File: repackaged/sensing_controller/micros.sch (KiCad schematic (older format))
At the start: 27 parts, among them J4 CONN_02X03, J5 CONN_02X03, U10 TXB0104, U7 ATMEGA16M1, U8 MCP2561-E_SN, U9 ATmega328P-AU, Y3 Crystal_SMD, Y4 Crystal_SMD

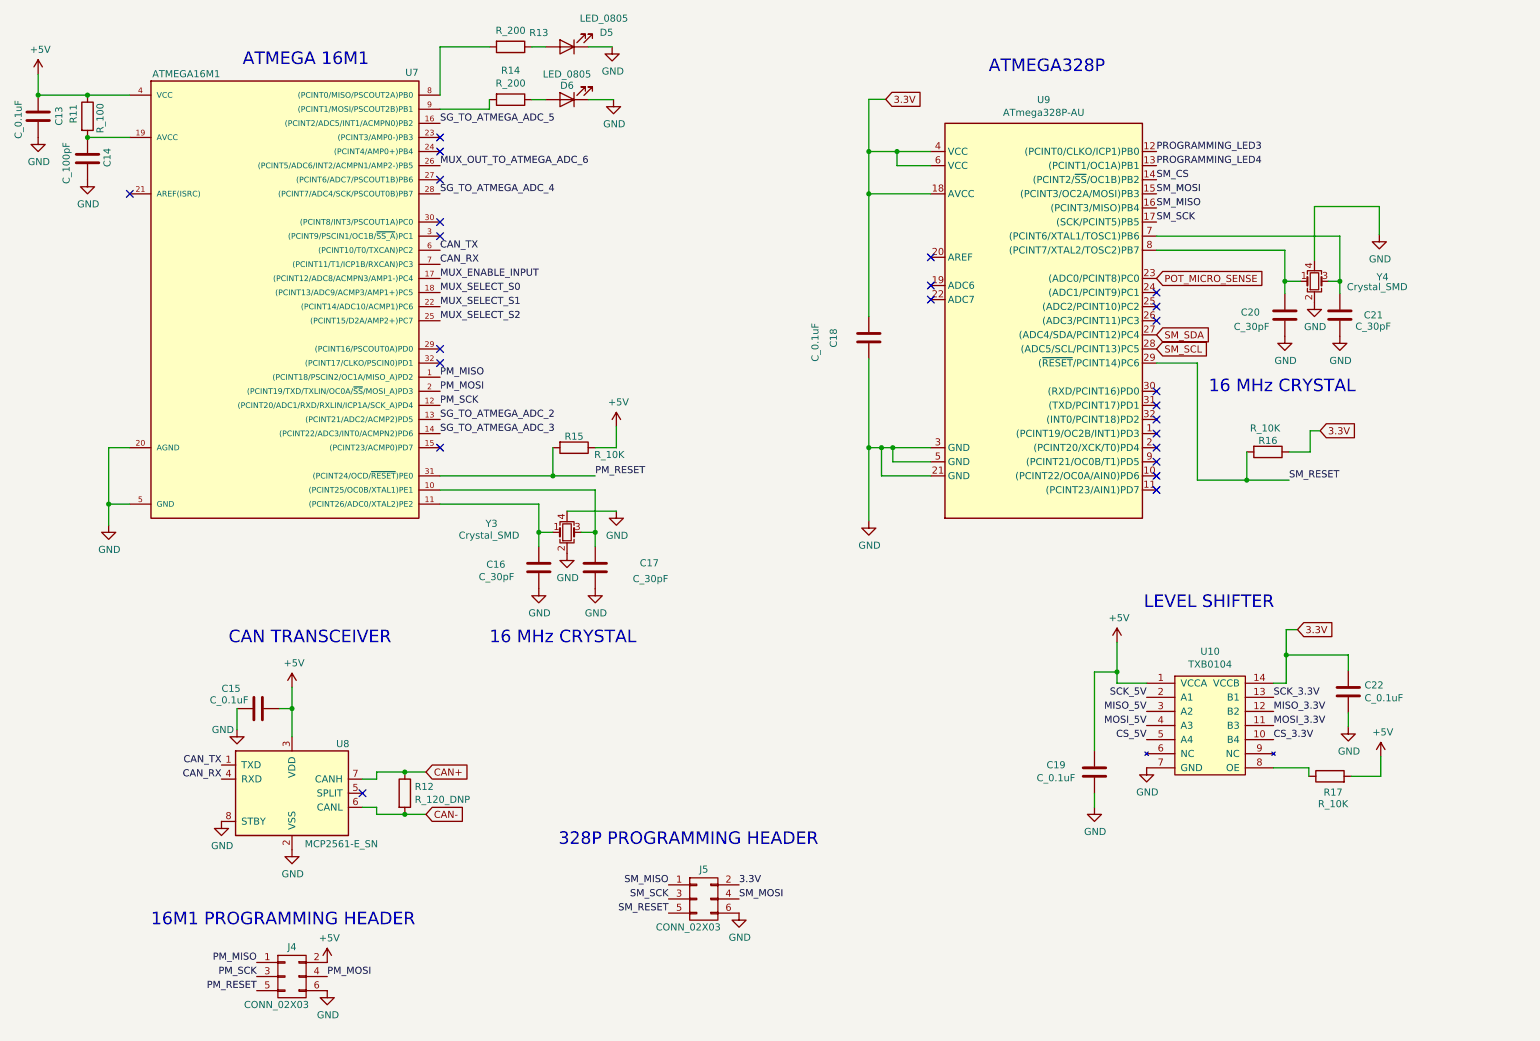
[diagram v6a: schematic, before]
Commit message: Fix net labels, clean schematic.
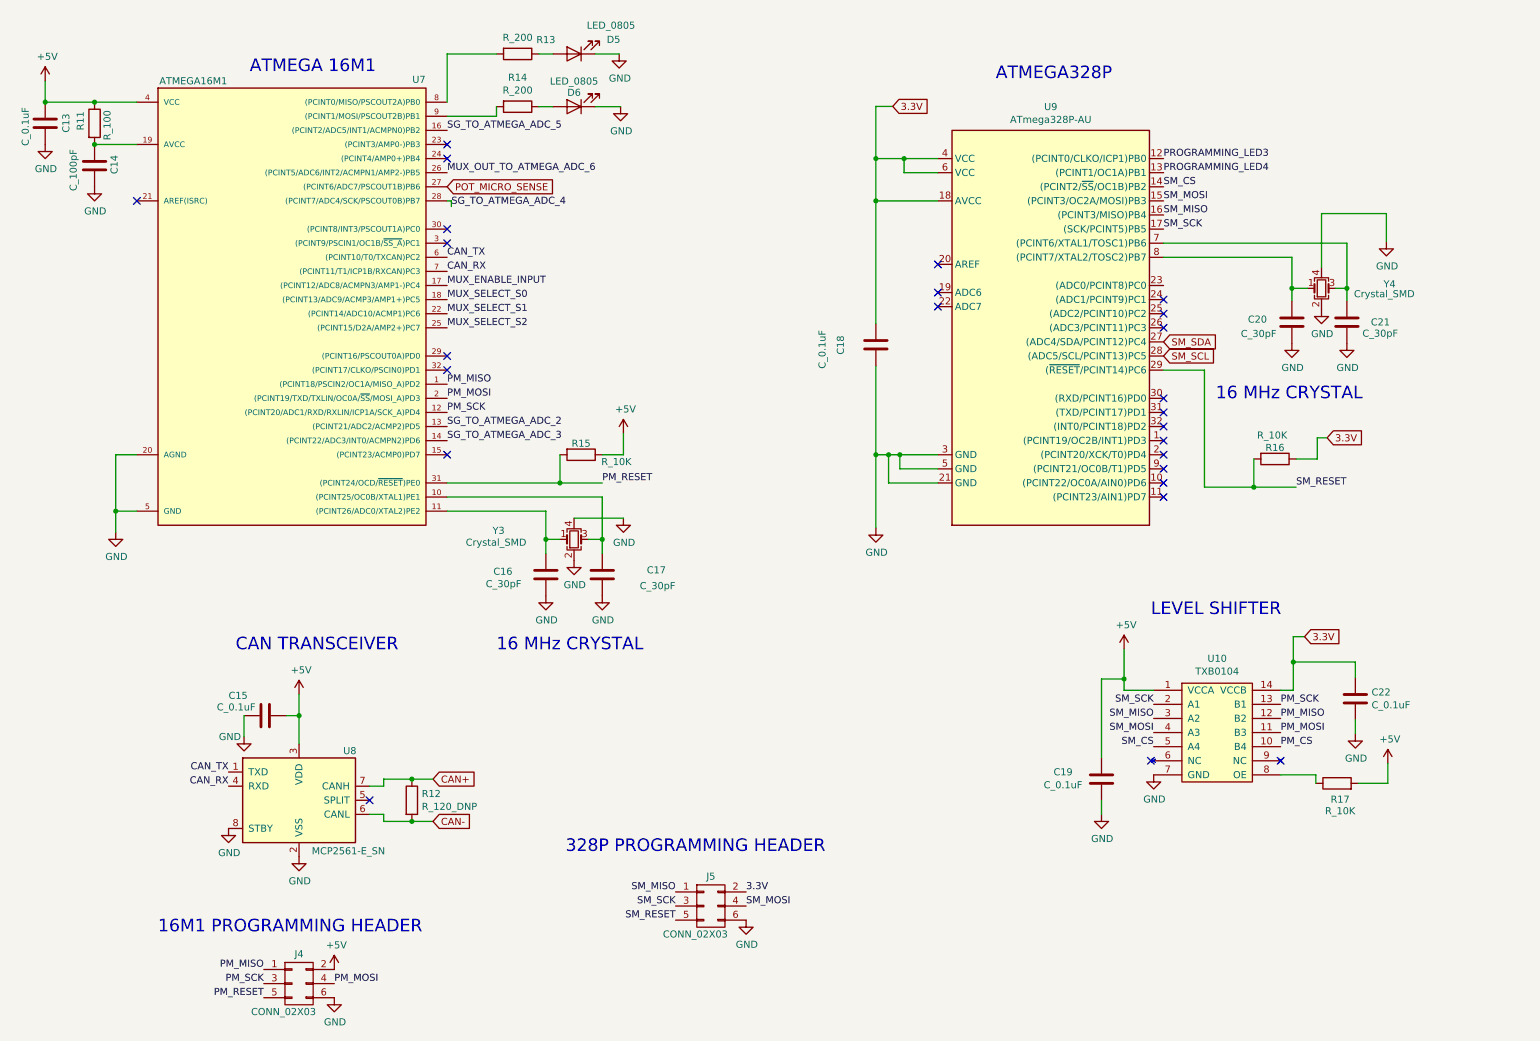
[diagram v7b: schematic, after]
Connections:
- net CS_5V is gone; now on net SM_CS: U10.5 (A4)
- net MISO_3.3V is gone; now on net PM_MISO: U10.12 (B2)
- net MISO_5V is gone; now on net SM_MISO: U10.3 (A2)
- net MOSI_3.3V is gone; now on net PM_MOSI: U10.11 (B3)
- net MOSI_5V is gone; now on net SM_MOSI: U10.4 (A3)
- net SCK_3.3V is gone; now on net PM_SCK: U10.13 (B1)
- net SCK_5V is gone; now on net SM_SCK: U10.2 (A1)
- net POT_MICRO_SENSE: now also U7.27 ((PCINT6/ADC7/PSCOUT1B)PB6); no longer U9.23 ((ADC0/PCINT8)PC0)
- net CS_3.3V renamed PM_CS
- no-connect marks 24 -> 25
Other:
- moved on the sheet: C13, C14, C15, C16, C17, C18, C19, C20, C21, C22, D5, D6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

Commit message: Fixed net labels and add missing components.
Changed power flags to global net labels, connected strain gauge nets to ATMEGA16M1, added LEDs where needed, and changed net labels to connect as needed.
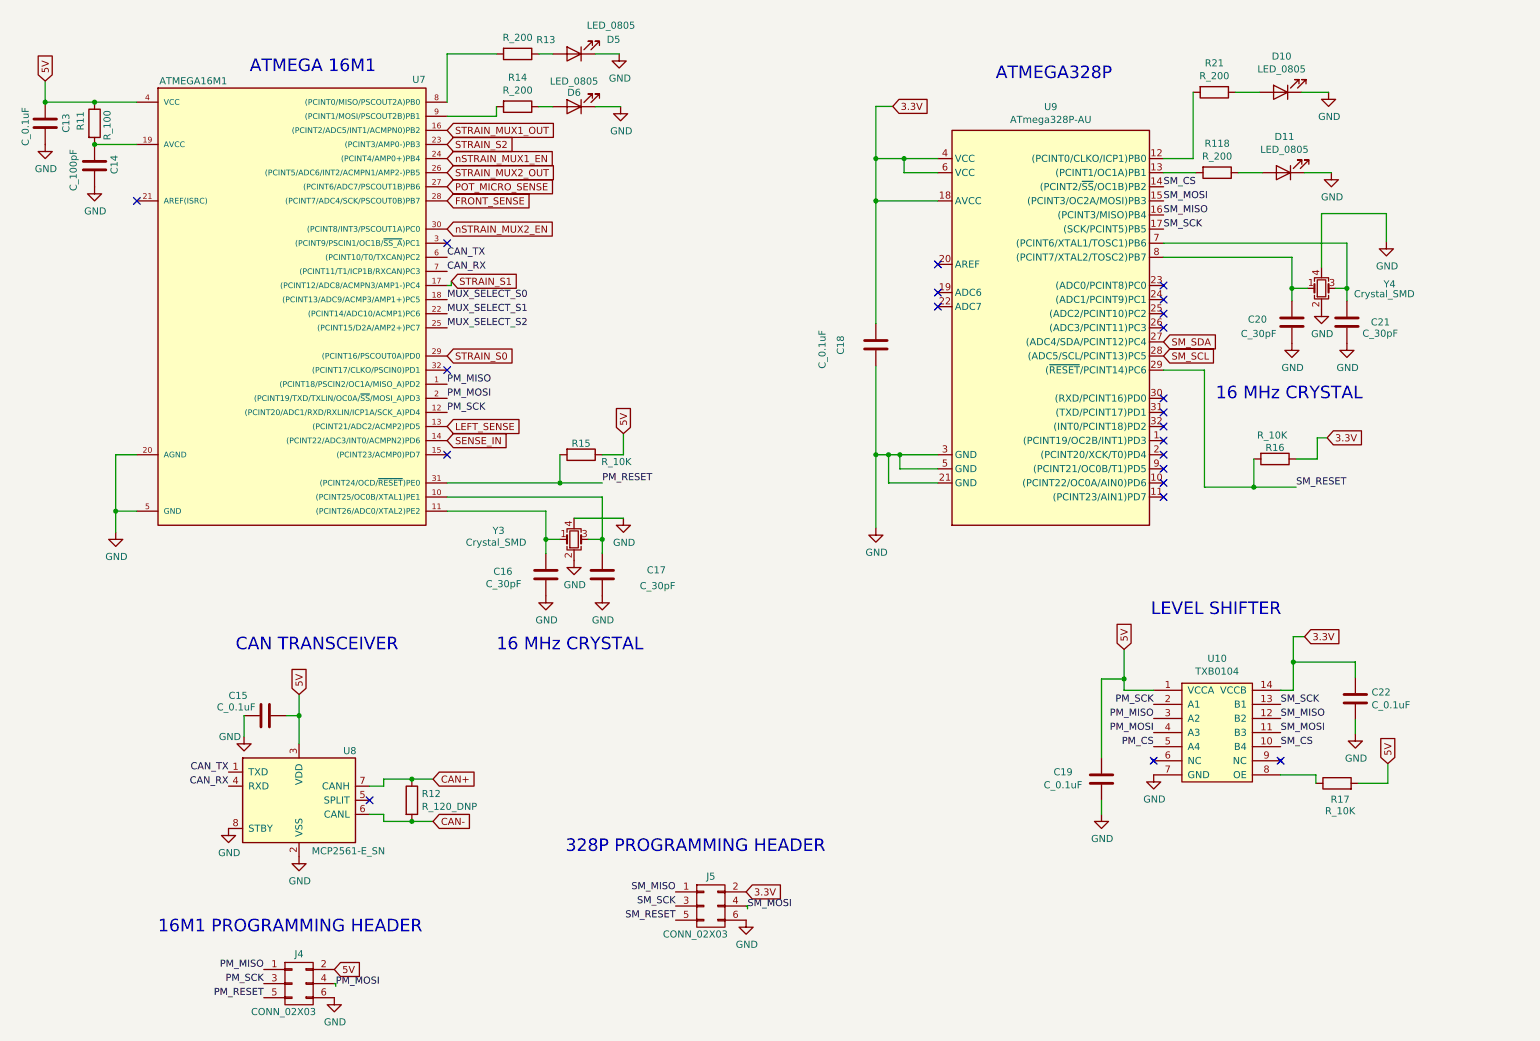
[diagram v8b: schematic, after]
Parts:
- added D10, D11: LED_0805, footprints:LED_0805_OEM, symbol formula:LED_0805
- added R118, R21: R_200, footprints:R_0805_OEM, symbol formula:R_200
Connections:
- net GND: now also D10.1 (K), D11.1 (K)
- net PM_CS: now also U10.5 (A4); no longer U10.10 (B4)
- net PM_MISO: now also U10.3 (A2); no longer U10.12 (B2)
- net PM_MOSI: now also U10.4 (A3); no longer U10.11 (B3)
- net PM_SCK: now also U10.2 (A1); no longer U10.13 (B1)
- net SM_CS: now also U10.10 (B4); no longer U10.5 (A4)
- net SM_MISO: now also U10.12 (B2); no longer U10.3 (A2)
- net SM_MOSI: now also U10.11 (B3); no longer U10.4 (A3)
- net SM_SCK: now also U10.13 (B1); no longer U10.2 (A1)
- net STRAIN_S2: now reaches U7.23 ((PCINT3/AMP0-)PB3)
- net nSTRAIN_MUX1_EN: now reaches U7.24 ((PCINT4/AMP0+)PB4)
- net STRAIN_S0: now reaches U7.29 ((PCINT16/PSCOUT0A)PD0)
- net nSTRAIN_MUX2_EN: now reaches U7.30 ((PCINT8/INT3/PSCOUT1A)PC0)
- net +5V renamed 5V
- net MUX_ENABLE_INPUT renamed STRAIN_S1
- net MUX_OUT_TO_ATMEGA_ADC_6 renamed STRAIN_MUX2_OUT
- net PROGRAMMING_LED3: no longer names the net of U9.12 ((PCINT0/CLKO/ICP1)PB0)
- net PROGRAMMING_LED3: now also R21.2
- net PROGRAMMING_LED4: no longer names the net of U9.13 ((PCINT1/OC1A)PB1)
- net PROGRAMMING_LED4: now also R118.2
- net SG_TO_ATMEGA_ADC_2 renamed LEFT_SENSE
- net SG_TO_ATMEGA_ADC_3 renamed SENSE_IN
- net SG_TO_ATMEGA_ADC_4 renamed FRONT_SENSE
- net SG_TO_ATMEGA_ADC_5 renamed STRAIN_MUX1_OUT
- new net: D11.2 (A), R118.1
- new net: D10.2 (A), R21.1
- no-connect marks 25 -> 22
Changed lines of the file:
@@
 Text Notes 9050 3270 0    89   ~ 0
 16 MHz CRYSTAL\n
-Text Label 8680 1550 0    50   ~ 0
-PROGRAMMING_LED3
-Text Label 8680 1650 0    50   ~ 0
-PROGRAMMING_LED4
 NoConn ~ 8680 3250
 NoConn ~ 8680 3350
@@
 Text Notes 3950 5050 0    89   ~ 0
 16 MHz CRYSTAL\n
-Wire Wire Line
-	1400 1450 1100 1450
 $Comp
 L formula:C_0.1uF C?
@@
 Wire Wire Line
 	1250 4200 1250 4050
-Wire Wire Line
-	1250 3650 1400 3650
-Wire Wire Line
-	1400 4050 1250 4050
 Connection ~ 1250 4050
 Wire Wire Line
@@
 Text Label 3600 2250 0    50   ~ 0
 CAN_TX
-$Comp
-L formula:ATMEGA16M1 U?
-U 1 1 60A4C28E
-P 2500 2850
-AR Path="/60A3DB07/60A4C28E" Ref="U?"  Part="1"
-AR Path="/60A3D93E/60A4C28E" Ref="U7"  Part="1"
-F 0 "U7" H 3400 4710 50  0000 C CNN
-F 1 "ATMEGA16M1" H 1800 4700 50  0000 C CNN
-F 2 "footprints:TQFP-32_7x7mm_Pitch0.8mm" H 2500 2850 50  0001 C CIN
-F 3 "http://ww1.microchip.com/downloads/en/DeviceDoc/Atmel-8209-8-bit%20AVR%20ATmega16M1-32M1-64M1_Datasheet.pdf" H 1550 4680 50  0001 C CNN
-F 4 "DK" H 2500 2850 60  0001 C CNN "MFN"
-F 5 "ATMEGA16M1-AU-ND" H 2500 2850 60  0001 C CNN "MPN"
-F 6 "https://www.digikey.com/product-detail/en/atmel/ATMEGA16M1-AU/ATMEGA16M1-AU-ND/2271208" H 1950 5080 60  0001 C CNN "PurchasingLink"
-	1    2500 2850
-	1    0    0    -1
-$EndComp
-Text Label 3600 3450 0    50   ~ 0
-SG_TO_ATMEGA_ADC_2
-Text Label 3600 3550 0    50   ~ 0
-SG_TO_ATMEGA_ADC_3
-Text Label 3600 1350 0    50   ~ 0
-SG_TO_ATMEGA_ADC_5
-Text Label 3600 1650 0    50   ~ 0
-MUX_OUT_TO_ATMEGA_ADC_6
-Text Label 3600 2450 0    50   ~ 0
-MUX_ENABLE_INPUT
 Text Label 3600 2550 0    50   ~ 0
 MUX_SELECT_S0
@@
 Wire Wire Line
 	4250 1182 4350 1182
-NoConn ~ 3600 1450
-NoConn ~ 3600 2950
 NoConn ~ 3600 3050
 NoConn ~ 3600 3650
-NoConn ~ 3600 2050
-NoConn ~ 3600 1550
 NoConn ~ 3600 2150
 Wire Wire Line
@@
 Text Label 2300 7500 2    50   ~ 0
 PM_RESET
-Text Label 2800 7400 0    50   ~ 0
+Text Label 2810 7420 0    50   ~ 0
 PM_MOSI
 $Comp
@@
 Text Label 5220 6950 2    50   ~ 0
 SM_RESET
-Text Label 5720 6850 0    50   ~ 0
+Text Label 5730 6870 0    50   ~ 0
 SM_MOSI
 $Comp
@@
 Text Notes 4440 6480 0    89   ~ 0
 328P PROGRAMMING HEADER\n
-Text Label 5720 6750 0    50   ~ 0
-3.3V
 Wire Wire Line
 	9510 5320 9600 5320
@@
 	10040 5530 10040 5630
 Text Label 9510 5420 0    50   ~ 0
-PM_SCK
+SM_SCK
 Wire Wire Line
 	9600 5120 10040 5120
 Text Label 9510 5520 0    50   ~ 0
-PM_MISO
+SM_MISO
 Text Label 9510 5620 0    50   ~ 0
-PM_MOSI
+SM_MOSI
 Text Label 9510 5720 0    50   ~ 0
-PM_CS
+SM_CS
 Wire Wire Line
 	8400 5030 8400 5240
 Text Label 8610 5420 2    50   ~ 0
-SM_SCK
+PM_SCK
 Text Label 8610 5520 2    50   ~ 0
-SM_MISO
-Text Label 8610 5720 2    50   ~ 0
-SM_CS
+PM_MISO
 Text Label 8610 5620 2    50   ~ 0
-SM_MOSI
+PM_MOSI
 Wire Wire Line
 	8400 5320 8610 5320
@@
 Connection ~ 750  1150
 Connection ~ 1100 1150
-Wire Wire Line
-	1100 1150 1400 1150
 Connection ~ 1100 1450
 Text GLabel 3600 1750 2    50   Input ~ 0
@@
 Wire Wire Line
 	6640 1180 6760 1180
-$Comp
-L power:+5V #PWR044
-U 1 1 61022A0F
-P 750 1000
-F 0 "#PWR044" H 750 850 50  0001 C CNN
-F 1 "+5V" H 765 1173 50  0000 C CNN
-F 2 "" H 750 1000 50  0001 C CNN
-F 3 "" H 750 1000 50  0001 C CNN
-	1    750  1000
-	1    0    0    -1
-$EndComp
-$Comp
-L power:+5V #PWR059
-U 1 1 6102A539
-P 4850 3500
-F 0 "#PWR059" H 4850 3350 50  0001 C CNN
-F 1 "+5V" H 4865 3673 50  0000 C CNN
-F 2 "" H 4850 3500 50  0001 C CNN
-F 3 "" H 4850 3500 50  0001 C CNN
-	1    4850 3500
-	1    0    0    -1
-$EndComp
 Wire Wire Line
 	10270 5840 10270 5980
-$Comp
-L power:+5V #PWR071
-U 1 1 6102D834
-P 10270 5840
-F 0 "#PWR071" H 10270 5690 50  0001 C CNN
-F 1 "+5V" H 10285 6013 50  0000 C CNN
-F 2 "" H 10270 5840 50  0001 C CNN
-F 3 "" H 10270 5840 50  0001 C CNN
-	1    10270 5840
-	1    0    0    -1
-$EndComp
-$Comp
-L power:+5V #PWR052
-U 1 1 6103E904
-P 2800 7300
-F 0 "#PWR052" H 2800 7150 50  0001 C CNN
-F 1 "+5V" H 2815 7473 50  0000 C CNN
-F 2 "" H 2800 7300 50  0001 C CNN
-F 3 "" H 2800 7300 50  0001 C CNN
-	1    2800 7300
-	1    0    0    -1
-$EndComp
-$Comp
-L power:+5V #PWR050
-U 1 1 61044ED6
-P 2550 5350
-F 0 "#PWR050" H 2550 5200 50  0001 C CNN
-F 1 "+5V" H 2565 5523 50  0000 C CNN
-F 2 "" H 2550 5350 50  0001 C CNN
-F 3 "" H 2550 5350 50  0001 C CNN
-	1    2550 5350
-	1    0    0    -1
-$EndComp
-$Comp
-L power:+5V #PWR064
-U 1 1 6104C577
-P 8400 5030
-F 0 "#PWR064" H 8400 4880 50  0001 C CNN
-F 1 "+5V" H 8415 5203 50  0000 C CNN
-F 2 "" H 8400 5030 50  0001 C CNN
-F 3 "" H 8400 5030 50  0001 C CNN
-	1    8400 5030
-	1    0    0    -1
-$EndComp
 Wire Wire Line
 	3600 808  3600 1150
@@
 Wire Wire Line
 	3950 1250 3600 1250
-Text Label 3630 1890 0    50   ~ 0
-SG_TO_ATMEGA_ADC_4
-Wire Wire Line
-	3600 1850 3630 1850
-Wire Wire Line
-	3630 1850 3630 1890
 $Comp
 L formula:TXB0104 U?
@@
 $EndComp
 NoConn ~ 9510 5820
-NoConn ~ 8590 5820
+NoConn ~ 8610 5820
 Text GLabel 6760 1180 2    50   Input ~ 0
 3.3V
+Text GLabel 750  1000 1    50   Input ~ 0
+5V
+Text GLabel 4850 3500 1    50   Input ~ 0
+5V
+Text GLabel 8400 5030 1    50   Input ~ 0
+5V
+Text GLabel 10270 5840 1    50   Input ~ 0
+5V
+Text GLabel 5720 6750 2    50   Input ~ 0
+3.3V
+Wire Wire Line
+	5720 6850 5730 6850
+Wire Wire Line
+	5730 6850 5730 6870
+Text GLabel 2800 7300 2    50   Input ~ 0
+5V
+Wire Wire Line
+	2800 7400 2810 7400
+Wire Wire Line
+	2810 7400 2810 7420
+Text GLabel 2550 5350 1    50   Input ~ 0
+5V
+Text GLabel 3600 1350 2    50   Input ~ 0
+STRAIN_MUX1_OUT
+Text GLabel 3600 1650 2    50   Input ~ 0
+STRAIN_MUX2_OUT
+Text GLabel 3600 1550 2    50   Input ~ 0
+nSTRAIN_MUX1_EN
+Text GLabel 3600 2050 2    50   Input ~ 0
+nSTRAIN_MUX2_EN
+Text GLabel 3600 2950 2    50   Input ~ 0
+STRAIN_S0
+Text GLabel 3630 2420 2    50   Input ~ 0
+STRAIN_S1
+Wire Wire Line
+	3600 2450 3630 2450
+Wire Wire Line
+	3630 2450 3630 2420
+Wire Wire Line
+	1400 4050 1250 4050
+Wire Wire Line
+	1250 3650 1400 3650
+Wire Wire Line
+	1400 1450 1100 1450
+Wire Wire Line
+	1100 1150 1400 1150
+$Comp
+L formula:ATMEGA16M1 U?
+U 1 1 60A4C28E
+P 2500 2850
+AR Path="/60A3DB07/60A4C28E" Ref="U?"  Part="1"
+AR Path="/60A3D93E/60A4C28E" Ref="U7"  Part="1"
+F 0 "U7" H 3400 4710 50  0000 C CNN
+F 1 "ATMEGA16M1" H 1800 4700 50  0000 C CNN
+F 2 "footprints:TQFP-32_7x7mm_Pitch0.8mm" H 2500 2850 50  0001 C CIN
+F 3 "http://ww1.microchip.com/downloads/en/DeviceDoc/Atmel-8209-8-bit%20AVR%20ATmega16M1-32M1-64M1_Datasheet.pdf" H 1550 4680 50  0001 C CNN
+F 4 "DK" H 2500 2850 60  0001 C CNN "MFN"
+F 5 "ATMEGA16M1-AU-ND" H 2500 2850 60  0001 C CNN "MPN"
+F 6 "https://www.digikey.com/product-detail/en/atmel/ATMEGA16M1-AU/ATMEGA16M1-AU-ND/2271208" H 1950 5080 60  0001 C CNN "PurchasingLink"
+	1    2500 2850
+	1    0    0    -1
+$EndComp
+Text GLabel 3600 1450 2    50   Input ~ 0
+STRAIN_S2
+NoConn ~ 8680 2450
+Wire Wire Line
+	8680 1650 8910 1650
+$Comp
+L formula:R_200 R118
+U 1 1 61590DA3
+P 9060 1650
+F 0 "R118" V 8853 1650 50  0000 C CNN
+F 1 "R_200" V 8944 1650 50  0000 C CNN
+F 2 "footprints:R_0805_OEM" H 8990 1650 50  0001 C CNN
+F 3 "https://www.seielect.com/Catalog/SEI-RMCF_RMCP.pdf" H 9140 1650 50  0001 C CNN
+F 4 "DK" H 9060 1650 60  0001 C CNN "MFN"
+F 5 "RMCF0805JT200RCT-ND" H 9060 1650 60  0001 C CNN "MPN"
+F 6 "https://www.digikey.com/products/en?keywords=RMCF0805JT200RCT-ND" H 9540 2050 60  0001 C CNN "PurchasingLink"
+	1    9060 1650
+	0    1    1    0
+$EndComp
+$Comp
+L formula:LED_0805 D11
+U 1 1 61591DE2
+P 9530 1650
+F 0 "D11" H 9523 1395 50  0000 C CNN
+F 1 "LED_0805" H 9523 1486 50  0000 C CNN
+F 2 "footprints:LED_0805_OEM" H 9430 1650 50  0001 C CNN
+F 3 "http://www.osram-os.com/Graphics/XPic9/00078860_0.pdf" H 9530 1750 50  0001 C CNN
+F 4 "DK" H 9530 1650 60  0001 C CNN "MFN"
+F 5 "475-1410-1-ND" H 9530 1650 60  0001 C CNN "MPN"
+F 6 "https://www.digikey.com/products/en?keywords=475-1410-1-ND" H 9930 2150 60  0001 C CNN "PurchasingLink"
+	1    9530 1650
+	-1   0    0    1
+$EndComp
+Wire Wire Line
+	9210 1650 9380 1650
+$Comp
+L power:GND #PWR059
+U 1 1 615973B2
+P 9870 1650
+F 0 "#PWR059" H 9870 1400 50  0001 C CNN
+F 1 "GND" H 9875 1477 50  0000 C CNN
+F 2 "" H 9870 1650 50  0001 C CNN
+F 3 "" H 9870 1650 50  0001 C CNN
+	1    9870 1650
+	1    0    0    -1
+$EndComp
+Wire Wire Line
+	9680 1650 9870 1650
+$Comp
+L formula:R_200 R21
+U 1 1 615BFE17
+P 9040 1080
+F 0 "R21" V 8833 1080 50  0000 C CNN
+F 1 "R_200" V 8924 1080 50  0000 C CNN
+F 2 "footprints:R_0805_OEM" H 8970 1080 50  0001 C CNN
+F 3 "https://www.seielect.com/Catalog/SEI-RMCF_RMCP.pdf" H 9120 1080 50  0001 C CNN
+F 4 "DK" H 9040 1080 60  0001 C CNN "MFN"
+F 5 "RMCF0805JT200RCT-ND" H 9040 1080 60  0001 C CNN "MPN"
+F 6 "https://www.digikey.com/products/en?keywords=RMCF0805JT200RCT-ND" H 9520 1480 60  0001 C CNN "PurchasingLink"
+	1    9040 1080
+	0    1    1    0
+$EndComp
+$Comp
+L formula:LED_0805 D10
+U 1 1 615BFE20
+P 9510 1080
+F 0 "D10" H 9503 825 50  0000 C CNN
+F 1 "LED_0805" H 9503 916 50  0000 C CNN
+F 2 "footprints:LED_0805_OEM" H 9410 1080 50  0001 C CNN
+F 3 "http://www.osram-os.com/Graphics/XPic9/00078860_0.pdf" H 9510 1180 50  0001 C CNN
+F 4 "DK" H 9510 1080 60  0001 C CNN "MFN"
+F 5 "475-1410-1-ND" H 9510 1080 60  0001 C CNN "MPN"
+F 6 "https://www.digikey.com/products/en?keywords=475-1410-1-ND" H 9910 1580 60  0001 C CNN "PurchasingLink"
+	1    9510 1080
+	-1   0    0    1
+$EndComp
+Wire Wire Line
+	9190 1080 9360 1080
+$Comp
+L power:GND #PWR052
+U 1 1 615BFE27
+P 9850 1080
+F 0 "#PWR052" H 9850 830 50  0001 C CNN
+F 1 "GND" H 9855 907 50  0000 C CNN
+F 2 "" H 9850 1080 50  0001 C CNN
+F 3 "" H 9850 1080 50  0001 C CNN
+	1    9850 1080
+	1    0    0    -1
+$EndComp
+Wire Wire Line
+	9660 1080 9850 1080
+Wire Wire Line
+	8680 1550 8890 1550
+Wire Wire Line
+	8890 1550 8890 1080
+Text Label 8610 5720 2    50   ~ 0
+PM_CS
+Text GLabel 3600 1850 2    50   Input ~ 0
+FRONT_SENSE
+Text GLabel 3600 3450 2    50   Input ~ 0
+LEFT_SENSE
+Text GLabel 3600 3550 2    50   Input ~ 0
+SENSE_IN
 $EndSCHEMATC
